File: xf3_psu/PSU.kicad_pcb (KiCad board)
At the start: 2 copper layers, 76 x 50 mm, 25 parts, among them P1 CONN_01X03, P2 CONN_01X03, P3 xhole, P4 xhole, P5 xhole, P6 xhole, U3 LM78**, U4 LM79**

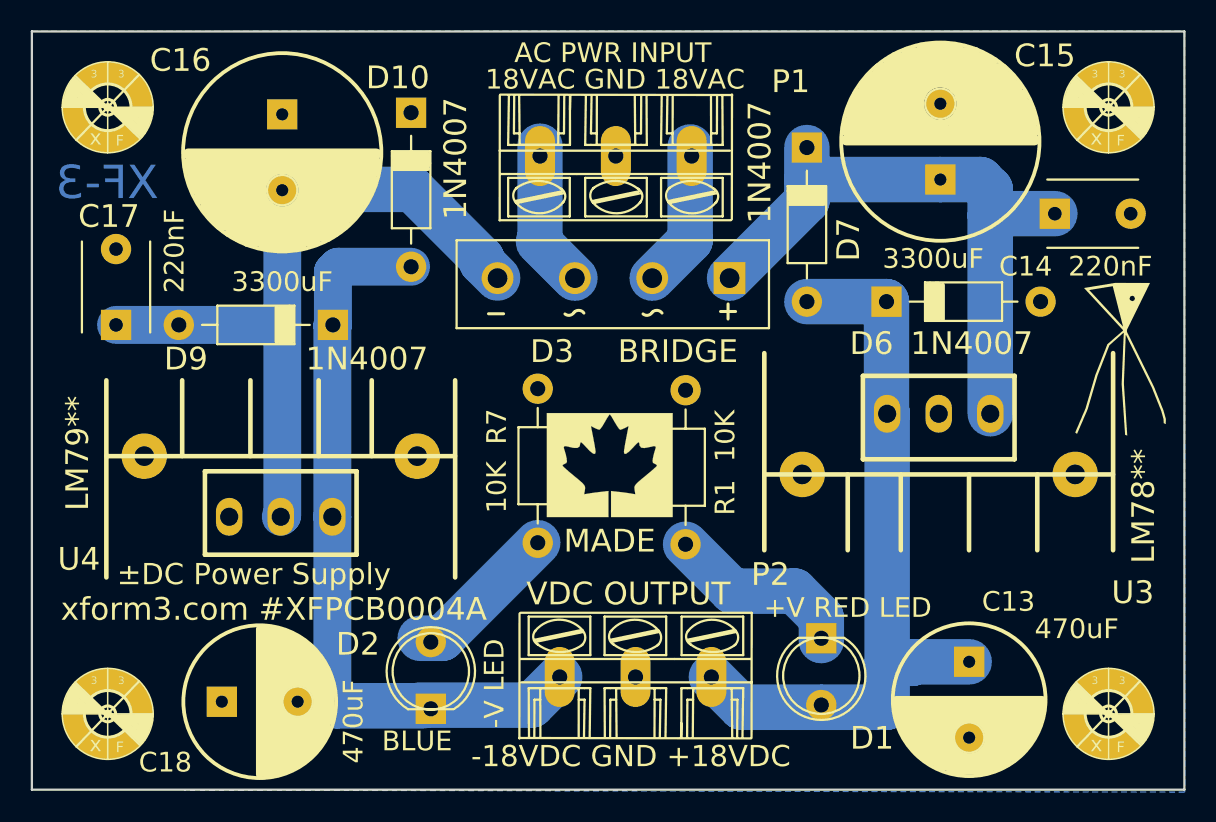
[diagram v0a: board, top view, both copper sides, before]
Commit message: fixed silk, changed graphics
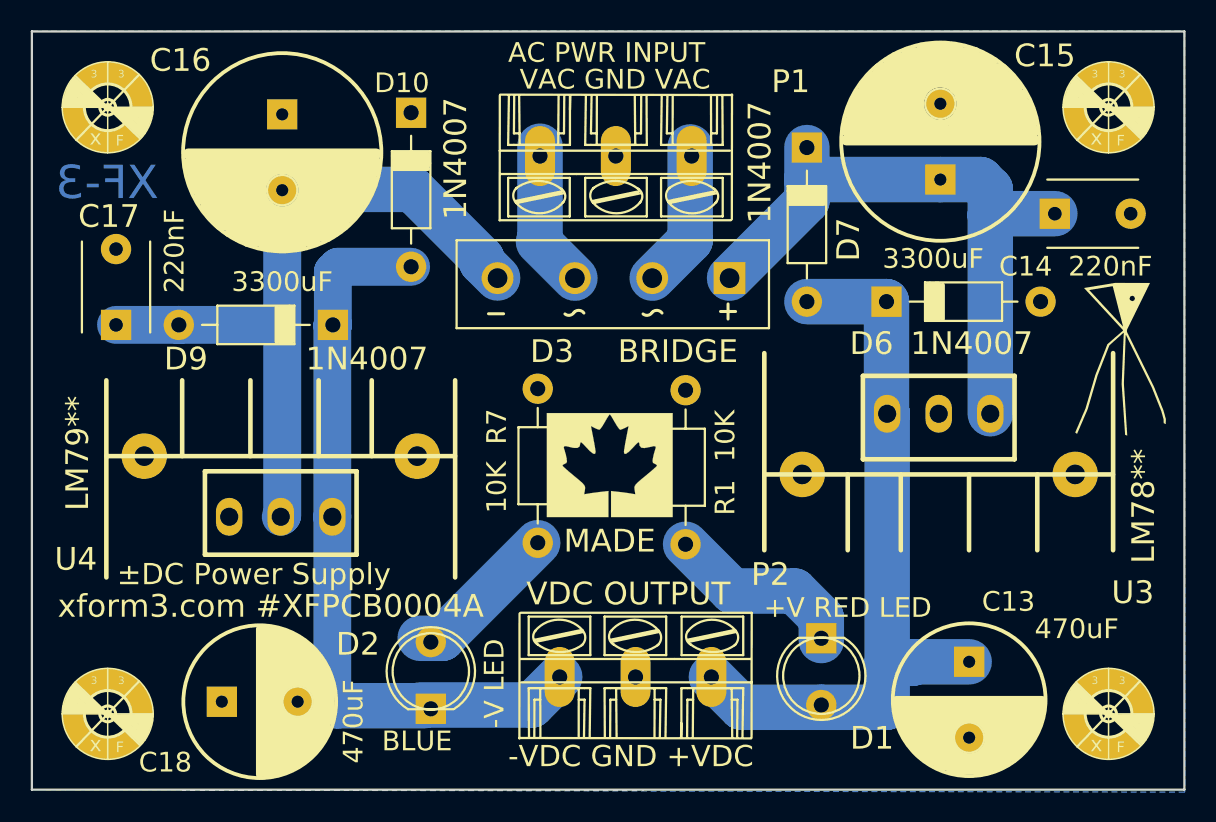
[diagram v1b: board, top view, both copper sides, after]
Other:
- board text added: "-VDC GND +VDC"
- board text added: "VAC GND VAC"
- board text removed: "-18VDC GND +18VDC"
- board text removed: "18VAC GND 18VAC"
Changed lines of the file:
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@@
     (descr "Diode, DO-41, SOD81, Horizontal, RM 10mm,")
     (tags "Diode, DO-41, SOD81, Horizontal, RM 10mm, 1N4007, SB140,")
-    (fp_text reference D10 (at -2.308 0.87546 540) (layer F.SilkS)
-      (effects (font (size 1.5 1.5) (thickness 0.15)))
+    (fp_text reference D10 (at -1.956 0.60546 360) (layer F.SilkS)
+      (effects (font (size 1.3 1.3) (thickness 0.15)))
     )
     (fp_text value 1N4007 (at 3.026 -2.93454 270) (layer F.SilkS)
@@
     (at 16.412 32.004)
     (descr "TO220, standard design, with 14°C/W heat sink")
-    (fp_text reference U4 (at -13.312 2.796) (layer F.SilkS)
+    (fp_text reference U4 (at -13.512 2.796) (layer F.SilkS)
       (effects (font (size 1.5 1.5) (thickness 0.2)))
     )
@@
     (effects (font (size 1.5 1.5) (thickness 0.2)) (justify left))
   )
-  (gr_text "AC PWR INPUT" (at 31.808 1.416) (layer F.SilkS)
+  (gr_text "AC PWR INPUT " (at 31.4 1.4) (layer F.SilkS)
     (effects (font (size 1.3 1.3) (thickness 0.2)) (justify left))
   )
-  (gr_text "xform3.com #XFPCB0004A\n" (at 1.9 38.1) (layer F.SilkS)
+  (gr_text "xform3.com #XFPCB0004A\n" (at 1.7 37.9) (layer F.SilkS)
     (effects (font (size 1.5 1.5) (thickness 0.2)) (justify left))
   )
-  (gr_text "18VAC GND 18VAC\n" (at 38.458 3.166) (layer F.SilkS)
+  (gr_text "VAC GND VAC\n" (at 38.458 3.166) (layer F.SilkS)
     (effects (font (size 1.3 1.3) (thickness 0.2)))
   )
-  (gr_text "-18VDC GND +18VDC\n" (at 39.5 47.8) (layer F.SilkS)
+  (gr_text "-VDC GND +VDC\n" (at 39.5 47.8) (layer F.SilkS)
     (effects (font (size 1.4 1.4) (thickness 0.2)))
   )
